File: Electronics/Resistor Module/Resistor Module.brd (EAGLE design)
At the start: 50 x 50 mm, 121 parts, among them U1 74HC595D, U2 74HC595D, U3 74HC595D, U4 74HC595D, U5 25AA010A

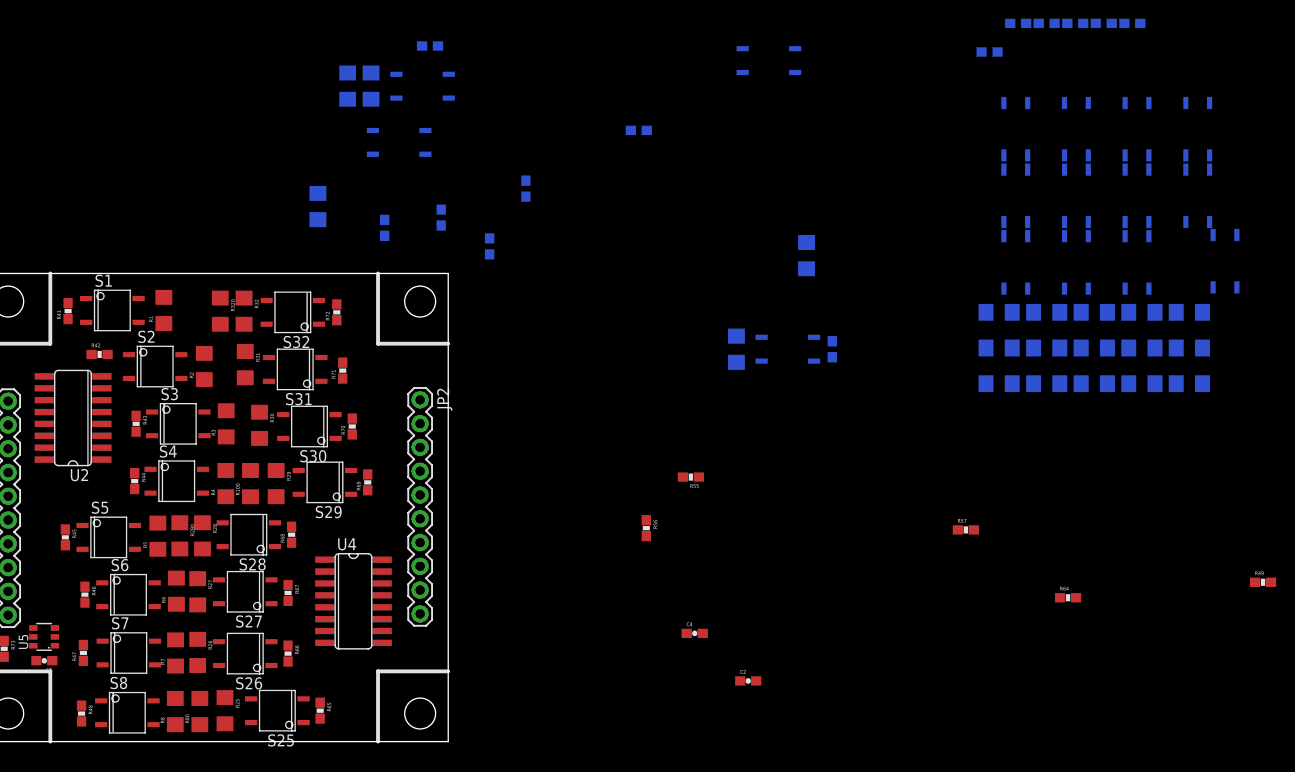
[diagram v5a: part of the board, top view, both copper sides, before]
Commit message: Placed all relays and critical resistors.
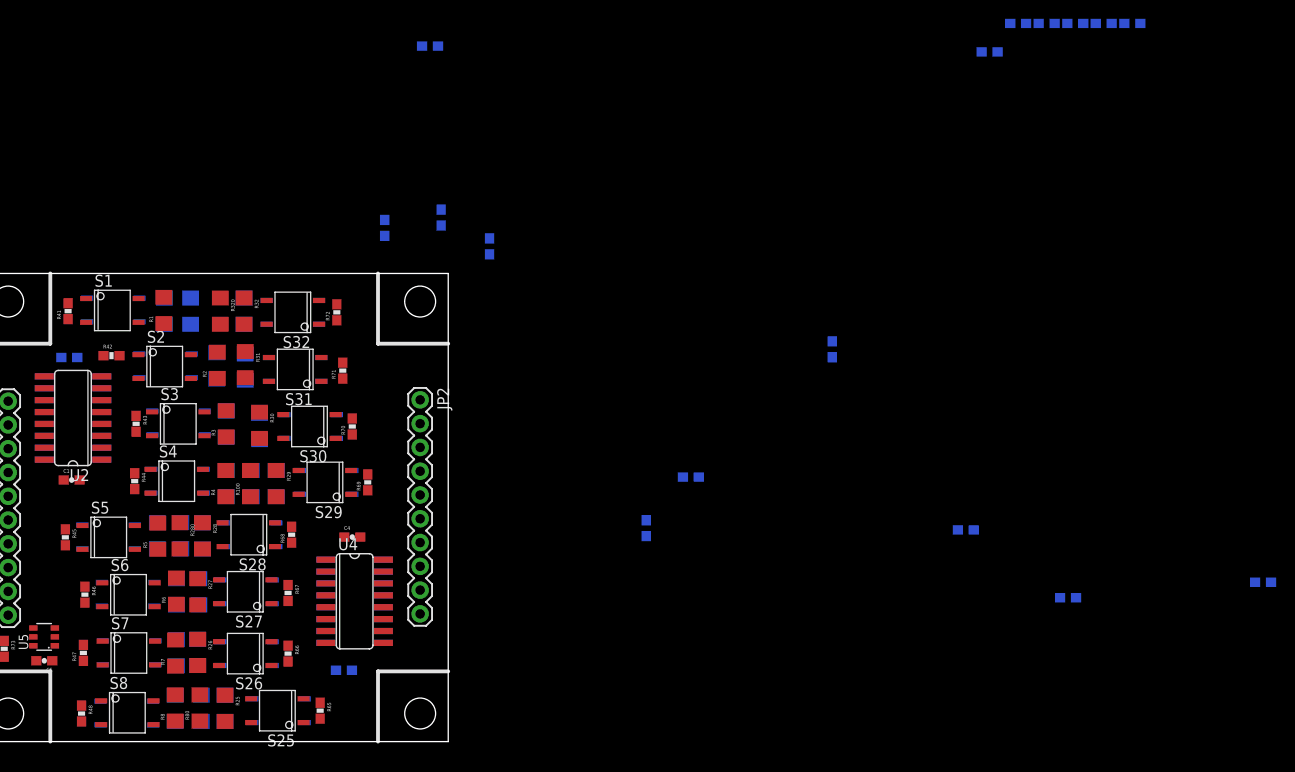
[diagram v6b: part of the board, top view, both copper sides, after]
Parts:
- moved S16 117.4 mm to (14.2, 46.1), turned to 90 degrees
- moved S24 111.9 mm to (31.9, 3.30), turned to 270 degrees
- moved R240 111.1 mm to (23.6, 3.56), turned to 90 degrees
- moved R22 108.9 mm to (23.4, 16.0), turned to 90 degrees
- moved S15 106.8 mm to (19.8, 40.1), turned to 90 degrees
- moved R16 104.4 mm to (19.7, 46.0), turned to 270 degrees
- moved S23 103.9 mm to (28.4, 9.40), turned to 270 degrees
- moved R21 102.3 mm to (23.7, 22.0), turned to 90 degrees
- moved R17 101.0 mm to (28.2, 46.0), turned to 90 degrees
- moved S14 100.9 mm to (21.2, 34.0), turned to 90 degrees
- moved S20 98.0 mm to (37.0, 27.7), turned to 270 degrees
- moved S13 97.1 mm to (21.1, 27.8), turned to 90 degrees
- moved R160 96.8 mm to (22.5, 46.0), turned to 270 degrees
- moved R200 95.7 mm to (29.0, 27.6), turned to 90 degrees
- moved S22 95.4 mm to (28.4, 16.0), turned to 270 degrees
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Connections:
- net 5V: now also C1.1, C2.1, U2.16; no longer C3.1, C4.1, U3.16
- net 5V_2: now also C3.1, C4.1, U3.16; no longer C1.1, C2.1, U2.16
- net GND: now also C1.2, C2.2, U2.8; no longer C3.2, C4.2, U3.8
- net GND_2: now also C3.2, C4.2, U3.8; no longer C1.2, C2.2, U2.8

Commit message: Everything in it's place
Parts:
- moved R49 126.9 mm to (10.9, 3.05), turned to 270 degrees
- moved R63 103.0 mm to (32.9, 9.40), turned to 270 degrees
- moved R62 101.3 mm to (32.9, 15.9), turned to 90 degrees
- moved R61 99.9 mm to (33.3, 22.1), turned to 90 degrees
- moved R59 93.7 mm to (39.9, 33.7), turned to 90 degrees
- moved R60 92.5 mm to (41.5, 27.7), turned to 90 degrees
- moved R64 80.8 mm to (36.3, 3.30), turned to 270 degrees
- moved R58 76.9 mm to (38.9, 39.6), turned to 90 degrees
- moved R54 74.9 mm to (16.6, 33.9)
- moved R50 74.5 mm to (11.3, 9.47), turned to 270 degrees
- moved R57 71.1 mm to (38.1, 45.8), turned to 90 degrees
- moved R56 66.0 mm to (9.36, 45.9), turned to 90 degrees
- moved R55 63.2 mm to (14.1, 41.2)
- moved R51 57.2 mm to (11.1, 15.6), turned to 270 degrees
- moved R52 47.5 mm to (9.12, 21.8), turned to 270 degrees
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
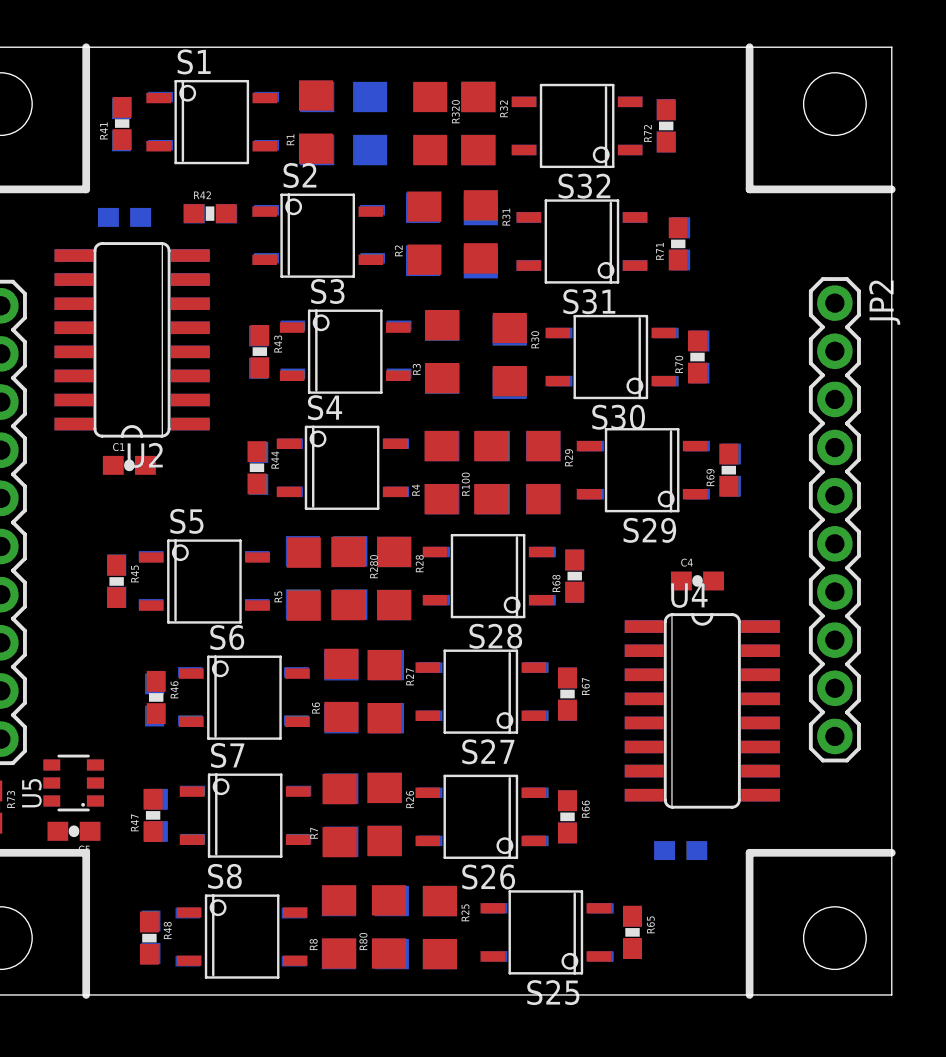
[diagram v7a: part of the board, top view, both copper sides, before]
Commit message: Routed main resistance path on both sides. Need to redo order on serial ports
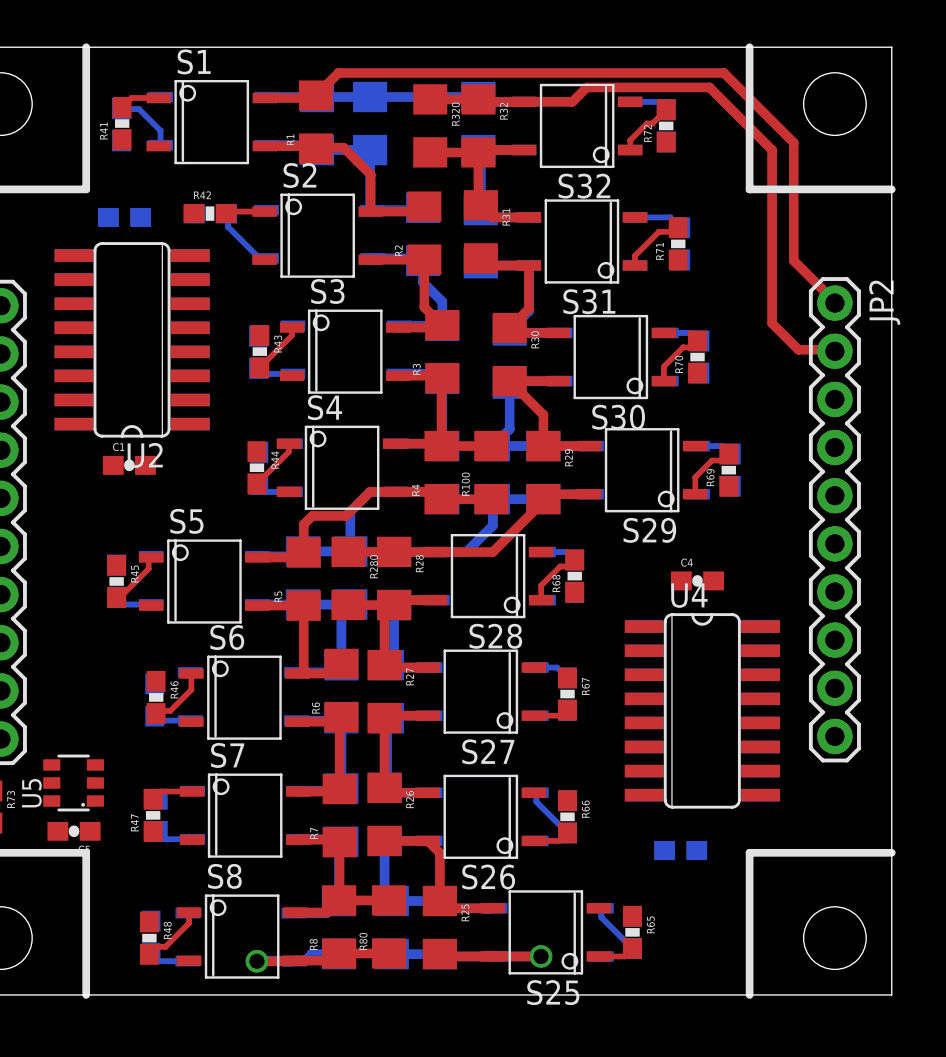
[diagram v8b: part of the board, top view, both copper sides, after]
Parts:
- moved R32 0.13 mm to (28.2, 45.8)
- moved R320 0.13 mm to (25.7, 45.8)
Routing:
- net R_IN: track 0.00 -> 39.3 mm
- net R_OUT: track 0.00 -> 32.8 mm
- net N$5: track 0.00 -> 14.8 mm
- net N$53: track 0.00 -> 14.0 mm
- net R160: track 0.00 -> 13.7 mm
- net R80: track 0.00 -> 13.5 mm, vias 0 -> 1
- net N$52: track 0.00 -> 13.3 mm, vias 0 -> 1
- net R120: track 0.00 -> 12.6 mm
- net N$47: track 0.00 -> 12.5 mm
- net N$46: track 0.00 -> 11.6 mm
- net N$42: track 0.00 -> 11.5 mm
- net N$50: track 0.00 -> 11.3 mm
- net N$25: track 0.00 -> 11.2 mm
- net N$4: track 0.00 -> 11.1 mm
- net N$15: track 0.00 -> 10.8 mm
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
